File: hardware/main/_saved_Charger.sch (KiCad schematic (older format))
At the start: 74 parts, among them K801 DIPxx-1Axx-13x, K802 SANYOU_SRD_Form_C, Q801 BCV27, Q802 Q_NPN_BEC, Q803 BCV27, U801 LM7812

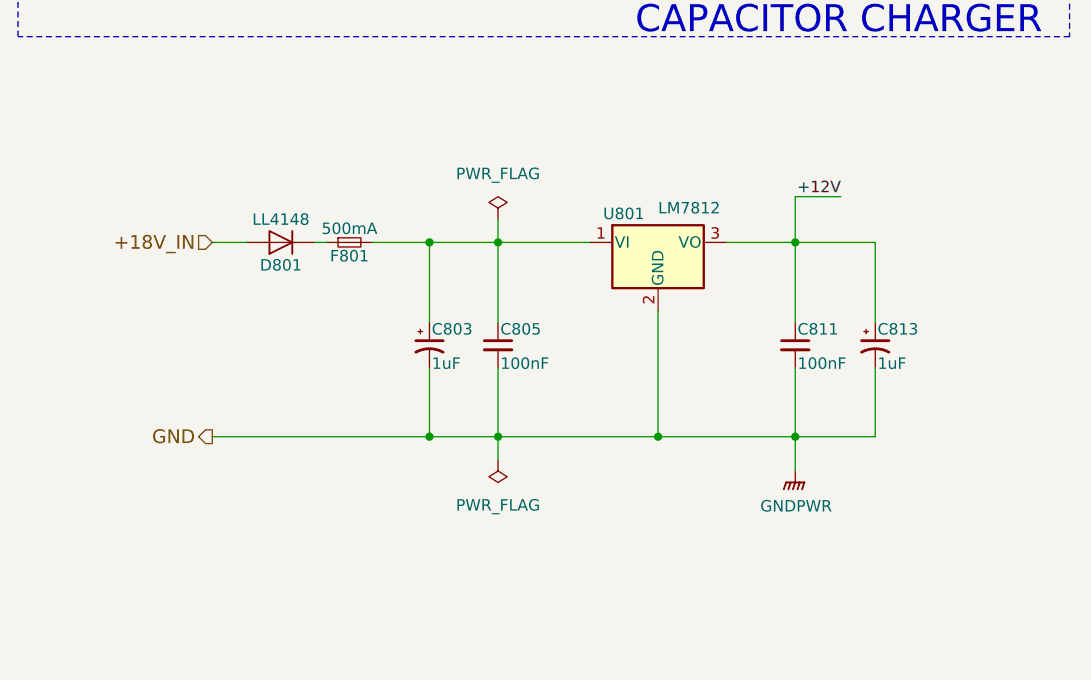
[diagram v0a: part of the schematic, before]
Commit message: Copper bar fixation
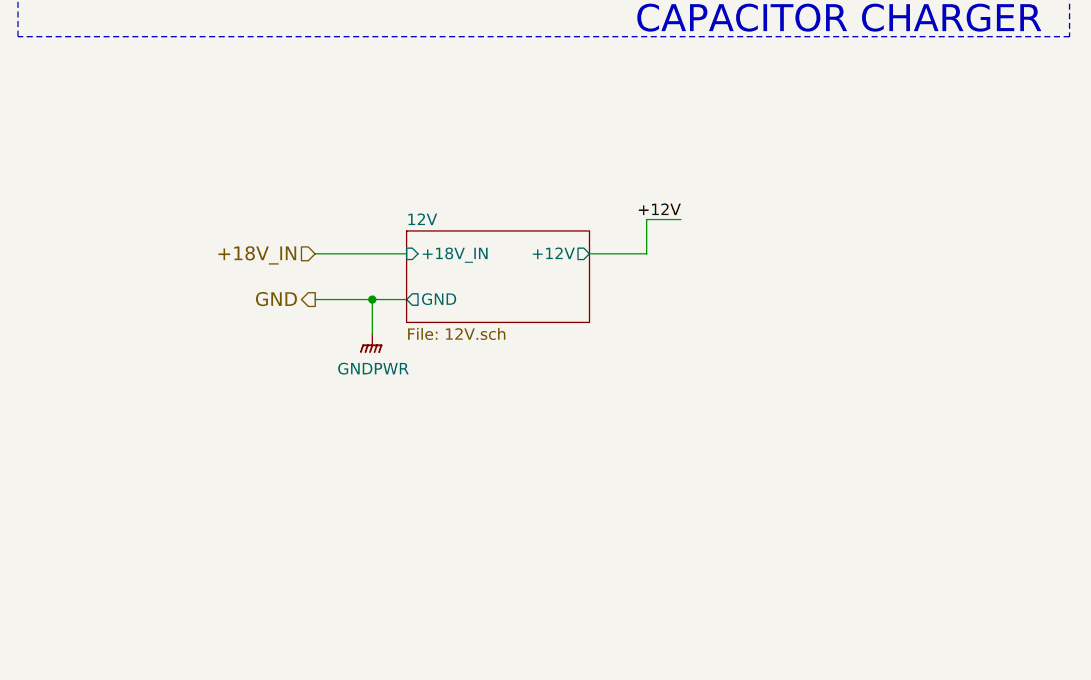
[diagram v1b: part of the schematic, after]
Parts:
- removed C803: 1uF, Capacitor_SMD:C_0805_2012Metric_Pad1.15x1.40mm_HandSolder, symbol Device:CP1_Small
- removed C805, C811: 100nF, Capacitor_SMD:C_0805_2012Metric_Pad1.15x1.40mm_HandSolder, symbol Device:C_Small
- removed C813: 1uF, Capacitor_Tantalum_SMD:CP_EIA-6032-20_AVX-F_Pad2.25x2.35mm_HandSolder, symbol Device:CP1_Small
- removed D801: LL4148, Diode_SMD:D_MiniMELF_Handsoldering, symbol Diode:LL4148
- removed F801: 500mA, Fuse:Fuse_1206_3216Metric_Pad1.42x1.75mm_HandSolder, symbol Device:Fuse_Small
- removed U801: LM7812, Package_SO:SOIC-8_3.9x4.9mm_P1.27mm, symbol Regulator_Linear:LM7805_TO220
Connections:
- wire segments 171 -> 152
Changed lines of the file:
@@
 $Descr A3 16535 11693
 encoding utf-8
-Sheet 2 8
+Sheet 2 9
 Title ""
 Date ""
@@
 Wire Wire Line
 	2800 3100 2800 3450
-$Comp
-L Regulator_Linear:LM7805_TO220 U?
-U 1 1 5CB0F970
-P 3450 7600
-AR Path="/5AACFFEF/5CB0F970" Ref="U?"  Part="1"
-AR Path="/5CA4DC1F/5CA5A5C0/5CB0F970" Ref="U?"  Part="1"
-AR Path="/5C9C4D6B/5CB0F970" Ref="U801"  Part="1"
-AR Path="/5CBD2CE3/5CB0F970" Ref="U?"  Part="1"
-F 0 "U801" H 3300 7725 50  0000 C CNN
-F 1 "LM7812" H 3450 7750 50  0000 L CNN
-F 2 "Package_SO:SOIC-8_3.9x4.9mm_P1.27mm" H 3450 7825 50  0001 C CIN
-F 3 "https://www.sparkfun.com/datasheets/Components/LM7805.pdf" H 3450 7550 50  0001 C CNN
-	1    3450 7600
-	1    0    0    -1
-$EndComp
-Text HLabel 1500 8450 0    60   Output ~ 0
+Text HLabel 1950 7850 0    60   Output ~ 0
 GND
-$Comp
-L Device:C_Small C?
-U 1 1 5CB0F97E
-P 2750 8050
-AR Path="/5AACFFEF/5CB0F97E" Ref="C?"  Part="1"
-AR Path="/5CA4DC1F/5CA5A5C0/5CB0F97E" Ref="C?"  Part="1"
-AR Path="/5C9C4D6B/5CB0F97E" Ref="C805"  Part="1"
-AR Path="/5CBD2CE3/5CB0F97E" Ref="C?"  Part="1"
-F 0 "C805" H 2760 8120 50  0000 L CNN
-F 1 "100nF" H 2760 7970 50  0000 L CNN
-F 2 "Capacitor_SMD:C_0805_2012Metric_Pad1.15x1.40mm_HandSolder" H 2750 8050 50  0001 C CNN
-F 3 "" H 2750 8050 50  0001 C CNN
-	1    2750 8050
-	1    0    0    -1
-$EndComp
-$Comp
-L Diode:LL4148 D?
-U 1 1 5CB0F984
-P 1800 7600
-AR Path="/5AACFFEF/5CB0F984" Ref="D?"  Part="1"
-AR Path="/5CA4DC1F/5CA5A5C0/5CB0F984" Ref="D?"  Part="1"
-AR Path="/5C9C4D6B/5CB0F984" Ref="D801"  Part="1"
-AR Path="/5CBD2CE3/5CB0F984" Ref="D?"  Part="1"
-F 0 "D801" H 1800 7700 50  0000 C CNN
-F 1 "LL4148" H 1800 7500 50  0000 C CNN
-F 2 "Diode_SMD:D_MiniMELF_Handsoldering" H 1800 7425 50  0001 C CNN
-F 3 "https://www.vishay.com/docs/85557/ll4148.pdf" H 1800 7600 50  0001 C CNN
-	1    1800 7600
-	-1   0    0    1
-$EndComp
-Text HLabel 1500 7600 0    60   Input ~ 0
+Text HLabel 1950 7650 0    60   Input ~ 0
 +18V_IN
-$Comp
-L Device:C_Small C?
-U 1 1 5CB0F98B
-P 4050 8050
-AR Path="/5AACFFEF/5CB0F98B" Ref="C?"  Part="1"
-AR Path="/5CA4DC1F/5CA5A5C0/5CB0F98B" Ref="C?"  Part="1"
-AR Path="/5C9C4D6B/5CB0F98B" Ref="C811"  Part="1"
-AR Path="/5CBD2CE3/5CB0F98B" Ref="C?"  Part="1"
-F 0 "C811" H 4060 8120 50  0000 L CNN
-F 1 "100nF" H 4060 7970 50  0000 L CNN
-F 2 "Capacitor_SMD:C_0805_2012Metric_Pad1.15x1.40mm_HandSolder" H 4050 8050 50  0001 C CNN
-F 3 "" H 4050 8050 50  0001 C CNN
-	1    4050 8050
-	1    0    0    -1
-$EndComp
-$Comp
-L Device:Fuse_Small F?
-U 1 1 5CB0F997
-P 2100 7600
-AR Path="/5AACFFEF/5CB0F997" Ref="F?"  Part="1"
-AR Path="/5CA4DC1F/5CA5A5C0/5CB0F997" Ref="F?"  Part="1"
-AR Path="/5C9C4D6B/5CB0F997" Ref="F801"  Part="1"
-AR Path="/5CBD2CE3/5CB0F997" Ref="F?"  Part="1"
-F 0 "F801" H 2100 7540 50  0000 C CNN
-F 1 "500mA" H 2100 7660 50  0000 C CNN
-F 2 "Fuse:Fuse_1206_3216Metric_Pad1.42x1.75mm_HandSolder" H 2100 7600 50  0001 C CNN
-F 3 "https://www.mouser.com/datasheet/2/643/0ZCJ_Nov2016-1132002.pdf" H 2100 7600 50  0001 C CNN
-	1    2100 7600
-	1    0    0    -1
-$EndComp
-Wire Wire Line
-	2450 8450 2450 8150
-Connection ~ 2450 7600
-Wire Wire Line
-	2750 8150 2750 8450
-Connection ~ 2450 8450
-Connection ~ 2750 7600
-Wire Wire Line
-	1650 7600 1500 7600
-Connection ~ 2750 8450
-Wire Wire Line
-	3450 8450 3450 7900
-Wire Wire Line
-	4050 8450 4050 8150
-Connection ~ 3450 8450
-Connection ~ 4050 7600
-Wire Wire Line
-	1500 8450 2450 8450
-Wire Wire Line
-	4400 7600 4400 7950
-Wire Wire Line
-	4400 8450 4400 8150
-Connection ~ 4050 8450
-Wire Wire Line
-	2450 7600 2450 7950
-Wire Wire Line
-	2200 7600 2450 7600
-Wire Wire Line
-	2450 7600 2750 7600
-Wire Wire Line
-	2450 8450 2750 8450
-Wire Wire Line
-	2750 7600 2750 7950
-Wire Wire Line
-	2750 7600 3150 7600
-Wire Wire Line
-	2750 8450 2750 8550
-Wire Wire Line
-	2750 8450 3450 8450
-Wire Wire Line
-	3450 8450 4050 8450
-Wire Wire Line
-	4050 7600 4400 7600
-Wire Wire Line
-	4050 7600 4050 7950
-Wire Wire Line
-	4050 8450 4400 8450
-Wire Wire Line
-	1950 7600 2000 7600
-$Comp
-L power:PWR_FLAG #FLG?
-U 1 1 5CB0F9BC
-P 2750 7500
-AR Path="/5AACFFEF/5CB0F9BC" Ref="#FLG?"  Part="1"
-AR Path="/5CA4DC1F/5CA5A5C0/5CB0F9BC" Ref="#FLG?"  Part="1"
-AR Path="/5C9C4D6B/5CB0F9BC" Ref="#FLG0802"  Part="1"
-AR Path="/5CBD2CE3/5CB0F9BC" Ref="#FLG?"  Part="1"
-F 0 "#FLG0802" H 2750 7575 50  0001 C CNN
-F 1 "PWR_FLAG" H 2750 7700 50  0000 C CNN
-F 2 "" H 2750 7500 50  0001 C CNN
-F 3 "~" H 2750 7500 50  0001 C CNN
-	1    2750 7500
-	1    0    0    -1
-$EndComp
-$Comp
-L power:PWR_FLAG #FLG?
-U 1 1 5CB0F9C2
-P 2750 8550
-AR Path="/5AACFFEF/5CB0F9C2" Ref="#FLG?"  Part="1"
-AR Path="/5CA4DC1F/5CA5A5C0/5CB0F9C2" Ref="#FLG?"  Part="1"
-AR Path="/5C9C4D6B/5CB0F9C2" Ref="#FLG0803"  Part="1"
-AR Path="/5CBD2CE3/5CB0F9C2" Ref="#FLG?"  Part="1"
-F 0 "#FLG0803" H 2750 8625 50  0001 C CNN
-F 1 "PWR_FLAG" H 2750 8750 50  0000 C CNN
-F 2 "" H 2750 8550 50  0001 C CNN
-F 3 "~" H 2750 8550 50  0001 C CNN
-	1    2750 8550
-	-1   0    0    1
-$EndComp
-Wire Wire Line
-	2750 7500 2750 7600
-$Comp
-L Device:CP1_Small C?
-U 1 1 5CB0F978
-P 2450 8050
-AR Path="/5AACFFEF/5CB0F978" Ref="C?"  Part="1"
-AR Path="/5CA4DC1F/5CA5A5C0/5CB0F978" Ref="C?"  Part="1"
-AR Path="/5C9C4D6B/5CB0F978" Ref="C803"  Part="1"
-AR Path="/5CBD2CE3/5CB0F978" Ref="C?"  Part="1"
-F 0 "C803" H 2460 8120 50  0000 L CNN
-F 1 "1uF" H 2460 7970 50  0000 L CNN
-F 2 "Capacitor_SMD:C_0805_2012Metric_Pad1.15x1.40mm_HandSolder" H 2450 8050 50  0001 C CNN
-F 3 "" H 2450 8050 50  0001 C CNN
-	1    2450 8050
-	1    0    0    -1
-$EndComp
-$Comp
-L Device:CP1_Small C?
-U 1 1 5CB0F991
-P 4400 8050
-AR Path="/5AACFFEF/5CB0F991" Ref="C?"  Part="1"
-AR Path="/5CA4DC1F/5CA5A5C0/5CB0F991" Ref="C?"  Part="1"
-AR Path="/5C9C4D6B/5CB0F991" Ref="C813"  Part="1"
-AR Path="/5CBD2CE3/5CB0F991" Ref="C?"  Part="1"
-F 0 "C813" H 4410 8120 50  0000 L CNN
-F 1 "1uF" H 4410 7970 50  0000 L CNN
-F 2 "Capacitor_Tantalum_SMD:CP_EIA-6032-20_AVX-F_Pad2.25x2.35mm_HandSolder" H 4400 8050 50  0001 C CNN
-F 3 "" H 4400 8050 50  0001 C CNN
-	1    4400 8050
-	1    0    0    -1
-$EndComp
-Wire Wire Line
-	4250 7400 4050 7400
-Wire Wire Line
-	4050 7400 4050 7600
-Text Label 4250 7400 2    50   ~ 0
-+12V
 Wire Wire Line
 	7700 4900 7700 5250
-$Comp
-L power:GNDPWR #PWR0804
-U 1 1 5CB769FE
-P 4050 8600
-AR Path="/5C9C4D6B/5CB769FE" Ref="#PWR0804"  Part="1"
-AR Path="/5CBD2CE3/5CB769FE" Ref="#PWR?"  Part="1"
-F 0 "#PWR0804" H 4050 8400 50  0001 C CNN
-F 1 "GNDPWR" H 4054 8446 50  0000 C CNN
-F 2 "" H 4050 8550 50  0001 C CNN
-F 3 "" H 4050 8550 50  0001 C CNN
-	1    4050 8600
-	1    0    0    -1
-$EndComp
-Wire Wire Line
-	4050 8600 4050 8450
 $Comp
 L power:PWR_FLAG #FLG0801
@@
 Wire Wire Line
 	1950 2600 2050 2600
-Wire Wire Line
-	3750 7600 4050 7600
 $Comp
 L power:PWR_FLAG #FLG0101
@@
 	1    0    0    -1
 $EndComp
+$Sheet
+S 2350 7550 800  400
+U 5CA70307
+F0 "12V" 50
+F1 "12V.sch" 50
+F2 "+18V_IN" I L 2350 7650 50
+F3 "GND" O L 2350 7850 50
+F4 "+12V" O R 3150 7650 50
+$EndSheet
+Wire Wire Line
+	1950 7850 2200 7850
+$Comp
+L power:GNDPWR #PWR0101
+U 1 1 5CA8D58E
+P 2200 8000
+AR Path="/5C9C4D6B/5CA8D58E" Ref="#PWR0101"  Part="1"
+AR Path="/5CBD2CE3/5CA8D58E" Ref="#PWR?"  Part="1"
+F 0 "#PWR0101" H 2200 7800 50  0001 C CNN
+F 1 "GNDPWR" H 2204 7846 50  0000 C CNN
+F 2 "" H 2200 7950 50  0001 C CNN
+F 3 "" H 2200 7950 50  0001 C CNN
+	1    2200 8000
+	1    0    0    -1
+$EndComp
+Wire Wire Line
+	2200 8000 2200 7850
+Connection ~ 2200 7850
+Wire Wire Line
+	2200 7850 2350 7850
+Wire Wire Line
+	1950 7650 2350 7650
+Wire Wire Line
+	3150 7650 3400 7650
+Wire Wire Line
+	3400 7650 3400 7500
+Wire Wire Line
+	3400 7500 3550 7500
+Text Label 3550 7500 2    50   ~ 0
++12V
 $EndSCHEMATC
